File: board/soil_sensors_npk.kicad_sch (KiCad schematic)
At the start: 0 parts

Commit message: added NPK and soil sensors pt. 1
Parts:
- added Conn16: Molex_uF_D_04, MRDT_Connectors:MOLEX_uF_D_04_Horizontal, symbol MRDT_Connectors:Molex_uF_D_04
- added Conn9: Molex_SL_03, symbol MRDT_Connectors:Molex_SL_03
- added R5: 120, symbol Device:R_US
- added U6: MAX3485, Package_SO:SOIC-8_3.9x4.9mm_P1.27mm, symbol Interface_UART:MAX3485
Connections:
- new net: Conn16.2, R5.1, U6.6 (A)
- new net: Conn16.3, R5.2, U6.7 (B)
- new net +3.3V: U6.8 (VCC)
- new net +5V: Conn16.1
- new net DE: U6.3 (DE)
- new net DI: U6.4 (DI)
- new net GND: Conn16.4, U6.5 (GND)
- new net RE: U6.2 (~{RE})
- new net RO: U6.1 (RO)

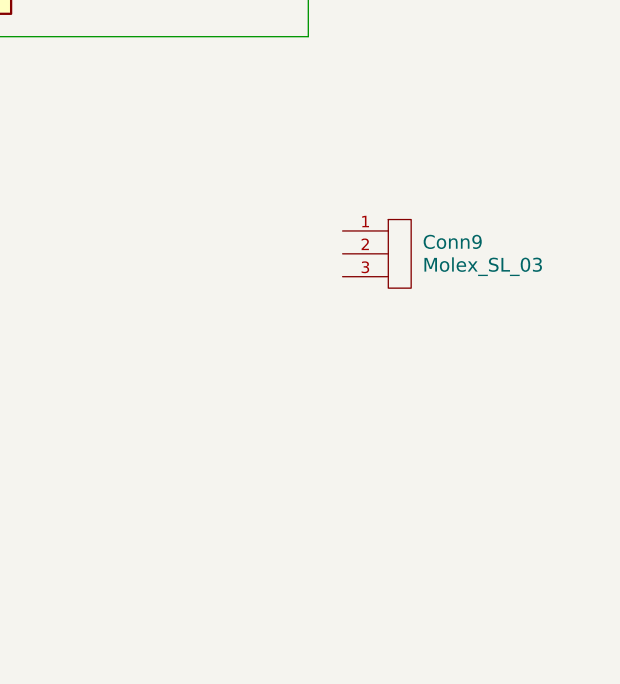
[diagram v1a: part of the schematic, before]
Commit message: Soil sensors pt. 2
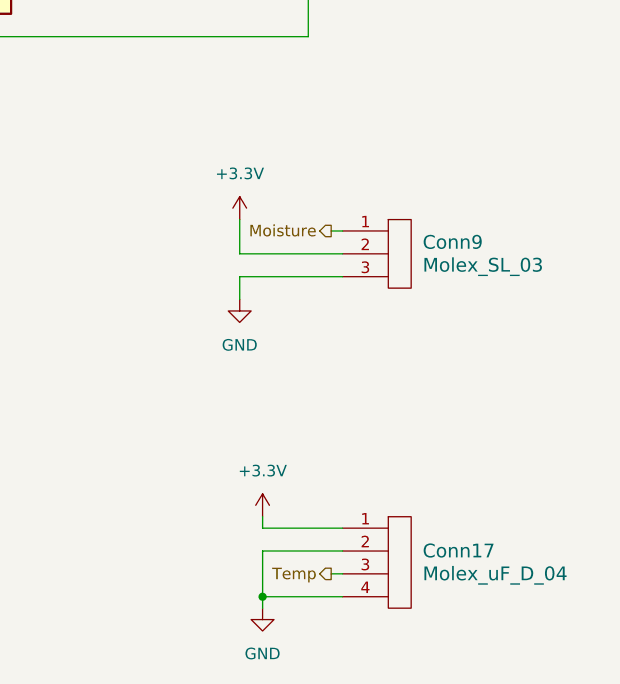
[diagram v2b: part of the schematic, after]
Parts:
- added Conn17: Molex_uF_D_04, MRDT_Connectors:MOLEX_uF_D_04_Horizontal, symbol MRDT_Connectors:Molex_uF_D_04
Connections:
- net +3.3V: now also Conn9.2, Conn17.1
- net GND: now also Conn9.3, Conn17.2, Conn17.4
- net Moisture: now reaches Conn9.1
- new net Temp: Conn17.3

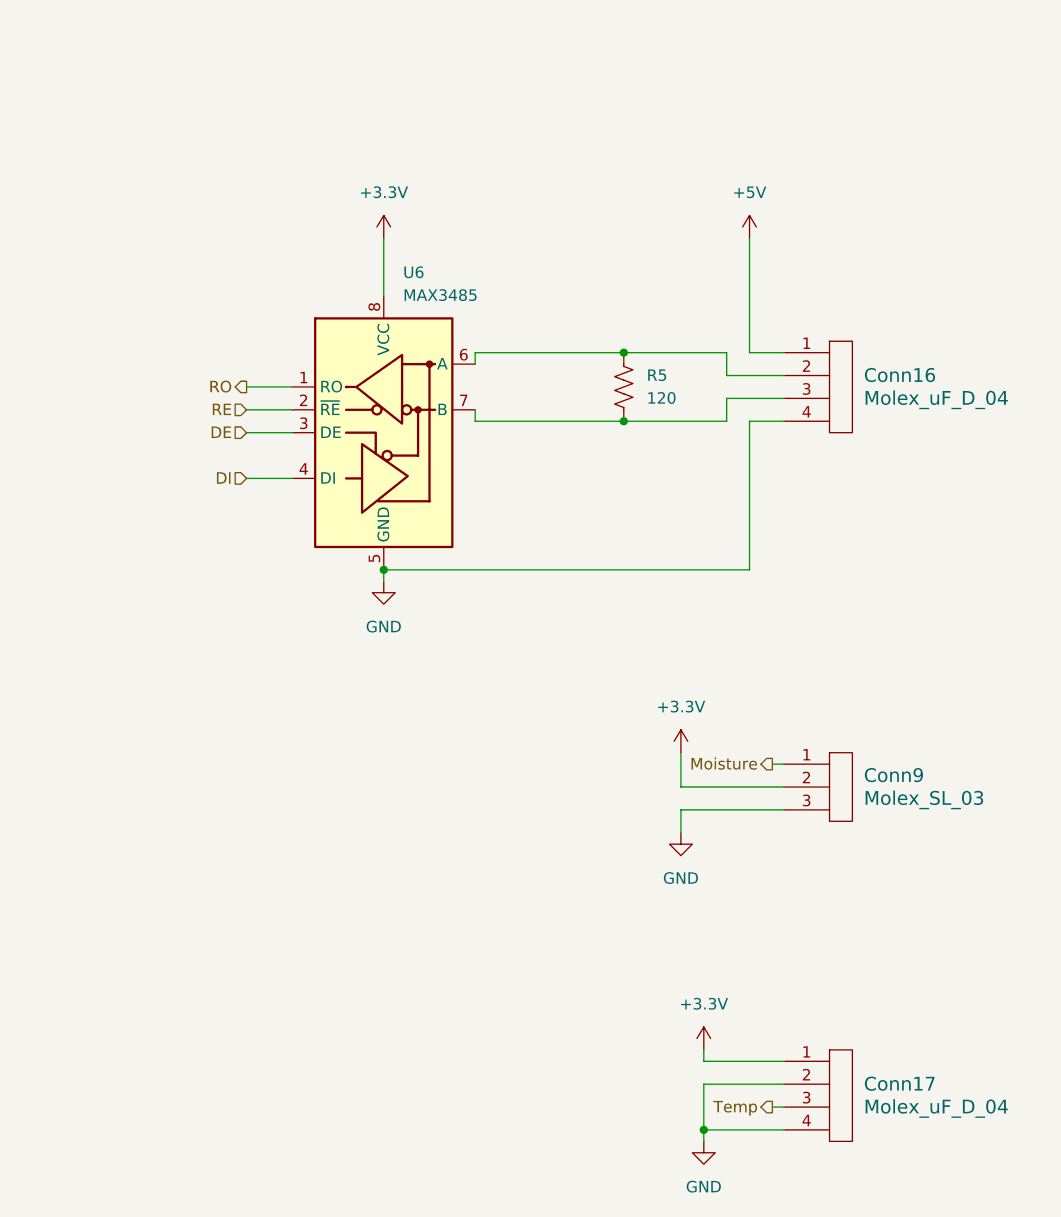
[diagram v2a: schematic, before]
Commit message: Added Labels, Missing Requirements, and Refined Look
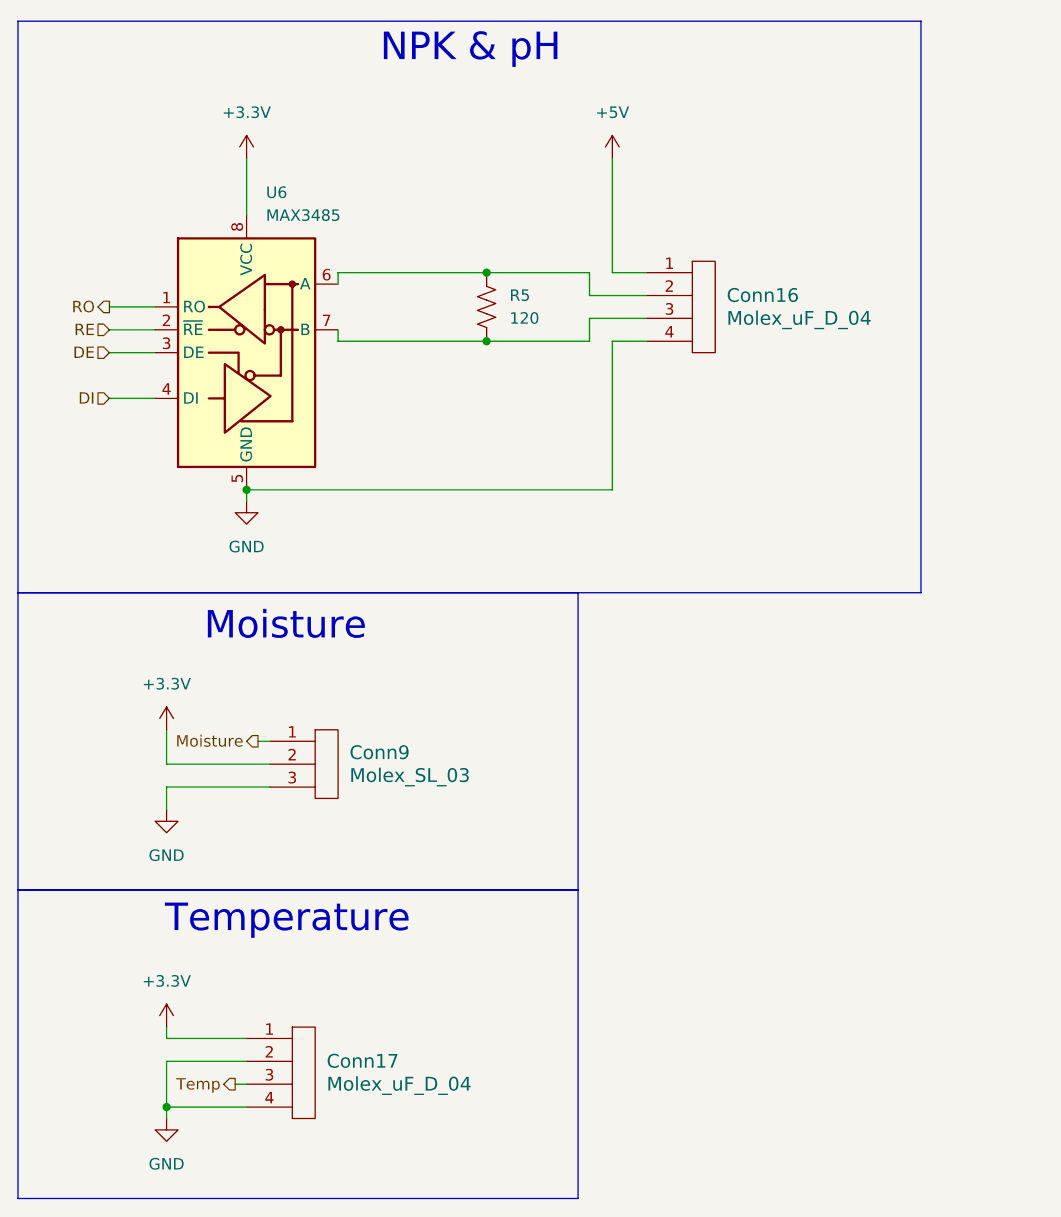
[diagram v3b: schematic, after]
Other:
- note added: "Moisture"
- note added: "NPK & pH"
- note added: "Temperature"
- moved on the sheet: Conn16, Conn17, Conn9, R5, U6

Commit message: assigned footprints
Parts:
- Conn9: footprint (none) -> MRDT_Connectors:MOLEX_SL_03_Vertical
- R5: footprint (none) -> Resistor_SMD:R_0603_1608Metric_Pad0.98x0.95mm_HandSolder
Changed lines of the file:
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@@
 			)
 		)
-		(property "Footprint" ""
+		(property "Footprint" "Resistor_SMD:R_0603_1608Metric_Pad0.98x0.95mm_HandSolder"
 			(at 65.786 44.704 90)
 			(effects
@@
 			)
 		)
-		(property "Footprint" ""
+		(property "Footprint" "MRDT_Connectors:MOLEX_SL_03_Vertical"
 			(at 45.72 99.06 0)
 			(effects

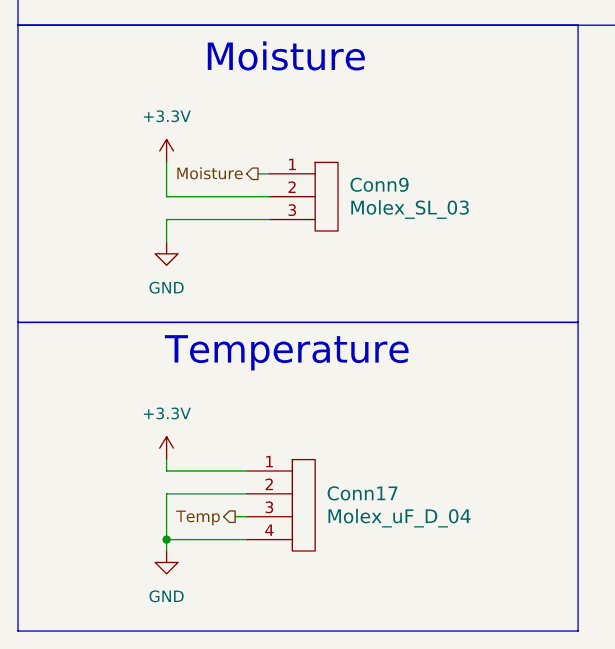
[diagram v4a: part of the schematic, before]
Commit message: Fixed issues after schematic review
added 6 leds for every servo, changed txd and rxd to pins 30/31, added additional oki for 3.3V
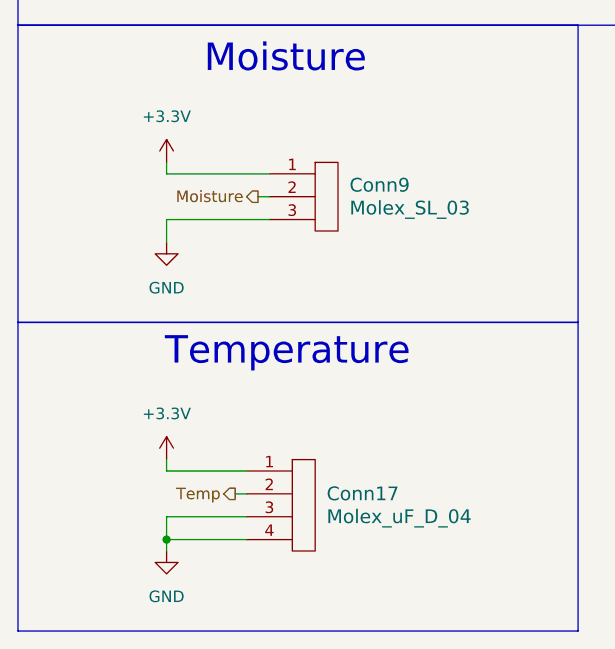
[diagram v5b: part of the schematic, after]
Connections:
- net +3.3V: now also Conn9.1; no longer Conn9.2
- net GND: now also Conn17.3; no longer Conn17.2
- net Moisture: now also Conn9.2; no longer Conn9.1
- net Temp: now also Conn17.2; no longer Conn17.3
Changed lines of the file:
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@@
+	)
+	(junction
+		(at 64.77 40.64)
+		(diameter 0)
+		(color 0 0 0 0)
 	)
 	(junction
@@
 		(color 0 0 0 0)
 	)
-	(junction
-		(at 64.77 40.64)
-		(diameter 0)
-		(color 0 0 0 0)
-	)
 	(wire
 		(pts
@@
 	(wire
 		(pts
+			(xy 39.37 95.25) (xy 40.64 95.25)
+		)
+		(stroke
+			(width 0)
+			(type default)
+		)
+	)
+	(wire
+		(pts
 			(xy 76.2 40.64) (xy 64.77 40.64)
 		)
@@
 	(wire
 		(pts
-			(xy 38.1 128.27) (xy 29.21 128.27)
+			(xy 36.83 128.27) (xy 38.1 128.27)
+		)
+		(stroke
+			(width 0)
+			(type default)
+		)
+	)
+	(wire
+		(pts
+			(xy 29.21 92.71) (xy 40.64 92.71)
 		)
 		(stroke
@@
 	(wire
 		(pts
-			(xy 38.1 133.35) (xy 29.21 133.35)
-		)
-		(stroke
-			(width 0)
-			(type default)
-		)
-	)
-	(wire
-		(pts
 			(xy 22.86 49.53) (xy 27.94 49.53)
 		)
@@
 	(wire
 		(pts
-			(xy 29.21 95.25) (xy 29.21 91.44)
-		)
-		(stroke
-			(width 0)
-			(type default)
-		)
-	)
-	(wire
-		(pts
 			(xy 48.26 46.99) (xy 48.26 48.26)
 		)
@@
 	(wire
 		(pts
-			(xy 40.64 95.25) (xy 29.21 95.25)
-		)
-		(stroke
-			(width 0)
-			(type default)
-		)
-	)
-	(wire
-		(pts
 			(xy 38.1 27.94) (xy 38.1 34.29)
 		)
@@
 	(wire
 		(pts
+			(xy 29.21 130.81) (xy 29.21 133.35)
+		)
+		(stroke
+			(width 0)
+			(type default)
+		)
+	)
+	(wire
+		(pts
+			(xy 29.21 91.44) (xy 29.21 92.71)
+		)
+		(stroke
+			(width 0)
+			(type default)
+		)
+	)
+	(wire
+		(pts
 			(xy 40.64 97.79) (xy 29.21 97.79)
 		)
@@
 	(wire
 		(pts
+			(xy 29.21 133.35) (xy 38.1 133.35)
+		)
+		(stroke
+			(width 0)
+			(type default)
+		)
+	)
+	(wire
+		(pts
 			(xy 76.2 43.18) (xy 76.2 40.64)
 		)
@@
 	(wire
 		(pts
-			(xy 39.37 92.71) (xy 40.64 92.71)
+			(xy 38.1 130.81) (xy 29.21 130.81)
 		)
 		(stroke
@@
 	(wire
 		(pts
-			(xy 29.21 128.27) (xy 29.21 133.35)
-		)
-		(stroke
-			(width 0)
-			(type default)
-		)
-	)
-	(wire
-		(pts
 			(xy 76.2 43.18) (xy 82.55 43.18)
 		)
@@
 		(pts
 			(xy 22.86 46.99) (xy 27.94 46.99)
-		)
-		(stroke
-			(width 0)
-			(type default)
-		)
-	)
-	(wire
-		(pts
-			(xy 36.83 130.81) (xy 38.1 130.81)
 		)
 		(stroke
@@
 	(hierarchical_label "Temp"
 		(shape output)
-		(at 36.83 130.81 180)
+		(at 36.83 128.27 180)
 		(effects
 			(font
@@
 	(hierarchical_label "Moisture"
 		(shape output)
-		(at 39.37 92.71 180)
+		(at 39.37 95.25 180)
 		(effects
 			(font

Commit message: switched soil sensor ports and layout work
soil sensor ports in fact needed to be the way they were originally after looking into the sensors we are using. Also started moving different components on layout to their spots.
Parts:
- removed Conn17: Molex_uF_D_04, MRDT_Connectors:MOLEX_uF_D_04_Horizontal, symbol MRDT_Connectors:Molex_uF_D_04
- added J2: Conn_01x04_MountingPin, symbol Connector_Generic_MountingPin:Conn_01x04_MountingPin
- Conn16: footprint MRDT_Connectors:MOLEX_uF_D_04_Horizontal -> MRDT_Connectors:MOLEX_SL_04_Vertical
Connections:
- net +3.3V: now also Conn9.2, J2.1 (Pin_1); no longer Conn9.1
- net GND: now also J2.2 (Pin_2), J2.4 (Pin_4)
- net Moisture: now also Conn9.1; no longer Conn9.2
- net Temp: now also J2.3 (Pin_3)
- no-connect marks 0 -> 1
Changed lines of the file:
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@@
 		(color 0 0 0 0)
 	)
+	(no_connect
+		(at 43.18 138.43)
+	)
 	(wire
 		(pts
@@
 	(wire
 		(pts
-			(xy 39.37 95.25) (xy 40.64 95.25)
+			(xy 36.83 130.81) (xy 38.1 130.81)
+		)
+		(stroke
+			(width 0)
+			(type default)
+		)
+	)
+	(wire
+		(pts
+			(xy 39.37 92.71) (xy 40.64 92.71)
+		)
+		(stroke
+			(width 0)
+			(type default)
+		)
+	)
+	(wire
+		(pts
+			(xy 40.64 95.25) (xy 29.21 95.25)
 		)
 		(stroke
@@
 	(wire
 		(pts
-			(xy 36.83 128.27) (xy 38.1 128.27)
-		)
-		(stroke
-			(width 0)
-			(type default)
-		)
-	)
-	(wire
-		(pts
-			(xy 29.21 92.71) (xy 40.64 92.71)
-		)
-		(stroke
-			(width 0)
-			(type default)
-		)
-	)
-	(wire
-		(pts
 			(xy 38.1 125.73) (xy 29.21 125.73)
 		)
@@
 	(wire
 		(pts
+			(xy 38.1 128.27) (xy 29.21 128.27)
+		)
+		(stroke
+			(width 0)
+			(type default)
+		)
+	)
+	(wire
+		(pts
 			(xy 76.2 45.72) (xy 82.55 45.72)
 		)
@@
 	(wire
 		(pts
-			(xy 29.21 130.81) (xy 29.21 133.35)
-		)
-		(stroke
-			(width 0)
-			(type default)
-		)
-	)
-	(wire
-		(pts
-			(xy 29.21 91.44) (xy 29.21 92.71)
+			(xy 29.21 128.27) (xy 29.21 133.35)
+		)
+		(stroke
+			(width 0)
+			(type default)
+		)
+	)
+	(wire
+		(pts
+			(xy 29.21 91.44) (xy 29.21 95.25)
 		)
 		(stroke
@@
 	(wire
 		(pts
-			(xy 38.1 130.81) (xy 29.21 130.81)
-		)
-		(stroke
-			(width 0)
-			(type default)
-		)
-	)
-	(wire
-		(pts
 			(xy 78.74 48.26) (xy 82.55 48.26)
 		)
@@
 	(wire
 		(pts
-			(xy 76.2 48.26) (xy 76.2 45.72)
+			(xy 76.2 45.72) (xy 76.2 48.26)
 		)
 		(stroke
@@
 	(hierarchical_label "Temp"
 		(shape output)
-		(at 36.83 128.27 180)
+		(at 36.83 130.81 180)
 		(effects
 			(font
@@
 	(hierarchical_label "Moisture"
 		(shape output)
-		(at 39.37 95.25 180)
+		(at 39.37 92.71 180)
 		(effects
 			(font
@@
 			)
 		)
-		(property "Footprint" "MRDT_Connectors:MOLEX_uF_D_04_Horizontal"
+		(property "Footprint" "MRDT_Connectors:MOLEX_SL_04_Vertical"
 			(at 87.63 49.53 0)
 			(effects
@@
 				(path "/05fd3c2e-b986-4426-9c38-2a77d5c929de/f1c20728-7c40-49e0-910a-0c2b6b14cbc0"
 					(reference "Conn16")
-					(unit 1)
-				)
-			)
-		)
-	)
-	(symbol
-		(lib_id "MRDT_Connectors:Molex_uF_D_04")
-		(at 43.18 134.62 0)
-		(unit 1)
-		(exclude_from_sim no)
-		(in_bom yes)
-		(on_board yes)
-		(dnp no)
-		(fields_autoplaced yes)
-		(property "Reference" "Conn17"
-			(at 46.99 128.2699 0)
-			(effects
-				(font
-					(size 1.524 1.524)
-				)
-				(justify left)
-			)
-		)
-		(property "Value" "Molex_uF_D_04"
-			(at 46.99 130.8099 0)
-			(effects
-				(font
-					(size 1.524 1.524)
-				)
-				(justify left)
-			)
-		)
-		(property "Footprint" "MRDT_Connectors:MOLEX_uF_D_04_Horizontal"
-			(at 43.18 134.62 0)
-			(effects
-				(font
-					(size 1.524 1.524)
-				)
-				(hide yes)
-			)
-		)
-		(property "Datasheet" ""
-			(at 43.18 134.62 0)
-			(effects
-				(font
-					(size 1.524 1.524)
-				)
-				(hide yes)
-			)
-		)
-		(property "Description" ""
-			(at 43.18 134.62 0)
-			(effects
-				(font
-					(size 1.27 1.27)
-				)
-				(hide yes)
-			)
-		)
-		(pin "1"
-		)
-		(pin "2"
-		)
-		(pin "3"
-		)
-		(pin "4"
-		)
-		(instances
-			(project ""
-				(path "/05fd3c2e-b986-4426-9c38-2a77d5c929de/f1c20728-7c40-49e0-910a-0c2b6b14cbc0"
-					(reference "Conn17")
 					(unit 1)
 				)
@@
 					(unit 1)
 				)
+			)
+		)
+	)
+	(symbol
+		(lib_id "Connector_Generic_MountingPin:Conn_01x04_MountingPin")
+		(at 43.18 128.27 0)
+		(unit 1)
+		(exclude_from_sim no)
+		(in_bom yes)
+		(on_board yes)
+		(dnp no)
+		(fields_autoplaced yes)
+		(property "Reference" "J2"
+			(at 45.72 128.6255 0)
+			(effects
+				(font
+					(size 1.27 1.27)
+				)
+				(justify left)
+			)
+		)
+		(property "Value" "Conn_01x04_MountingPin"
+			(at 45.72 131.1655 0)
+			(effects
+				(font
+					(size 1.27 1.27)
+				)
+				(justify left)
+			)
+		)
+		(property "Footprint" ""
+			(at 43.18 128.27 0)
+			(effects
+				(font
+					(size 1.27 1.27)
+				)
+				(hide yes)
+			)
+		)
+		(property "Datasheet" "~"
+			(at 43.18 128.27 0)
+			(effects
+				(font
+					(size 1.27 1.27)
+				)
+				(hide yes)
+			)
+		)
+		(property "Description" "Generic connectable mounting pin connector, single row, 01x04, script generated (kicad-library-utils/schlib/autogen/connector/)"
+			(at 43.18 128.27 0)
+			(effects
+				(font
+					(size 1.27 1.27)
+				)
+				(hide yes)
+			)
+		)
+		(pin "1"
+		)
+		(pin "2"
+		)
+		(pin "4"
+		)
+		(pin "3"
+		)
+		(pin "MP"
+		)
+		(instances
+			(project ""
+				(path "/05fd3c2e-b986-4426-9c38-2a77d5c929de/f1c20728-7c40-49e0-910a-0c2b6b14cbc0"
+					(reference "J2")
+					(unit 1)
+				)

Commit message: Layout Progress
Made a basic setup for locations, placed preliminary wires and text, rearranged teensy pins for simplicity
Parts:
- J2: footprint (none) -> Connector_PinHeader_2.54mm:PinHeader_1x04_P2.54mm_Vertical
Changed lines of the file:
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@@
 			)
 		)
-		(property "Footprint" ""
+		(property "Footprint" "Connector_PinHeader_2.54mm:PinHeader_1x04_P2.54mm_Vertical"
 			(at 43.18 128.27 0)
 			(effects

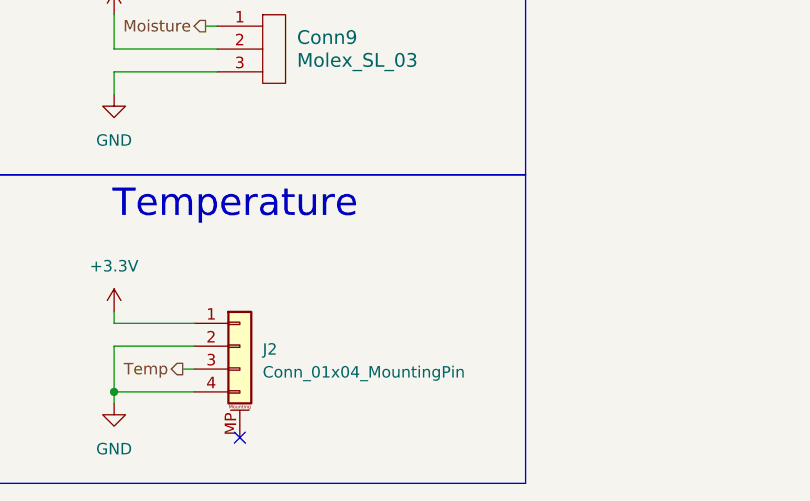
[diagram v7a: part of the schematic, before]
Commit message: Add reverse voltage protection circuit
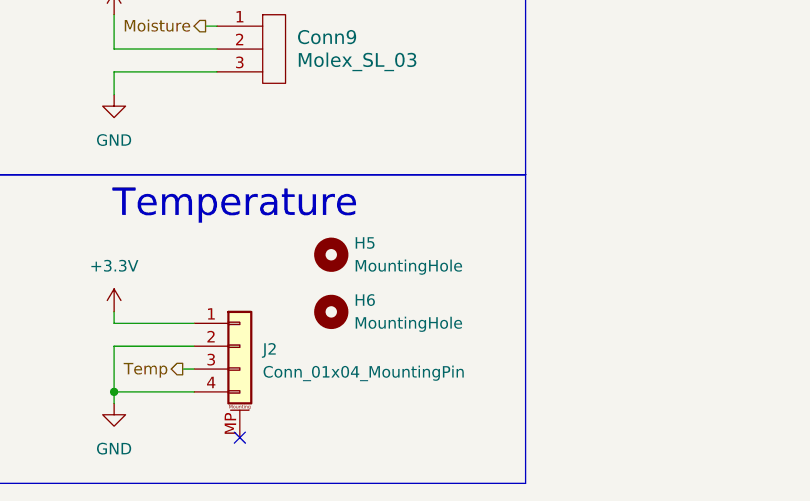
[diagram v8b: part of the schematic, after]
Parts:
- added H5, H6: MountingHole, MountingHole:MountingHole_2.7mm, symbol Mechanical:MountingHole
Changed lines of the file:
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@@
+	)
+	(symbol
+		(lib_id "Mechanical:MountingHole")
+		(at 53.34 124.46 0)
+		(unit 1)
+		(exclude_from_sim no)
+		(in_bom no)
+		(on_board yes)
+		(dnp no)
+		(fields_autoplaced yes)
+		(property "Reference" "H6"
+			(at 55.88 123.1899 0)
+			(effects
+				(font
+					(size 1.27 1.27)
+				)
+				(justify left)
+			)
+		)
+		(property "Value" "MountingHole"
+			(at 55.88 125.7299 0)
+			(effects
+				(font
+					(size 1.27 1.27)
+				)
+				(justify left)
+			)
+		)
+		(property "Footprint" "MountingHole:MountingHole_2.7mm"
+			(at 53.34 124.46 0)
+			(effects
+				(font
+					(size 1.27 1.27)
+				)
+				(hide yes)
+			)
+		)
+		(property "Datasheet" "~"
+			(at 53.34 124.46 0)
+			(effects
+				(font
+					(size 1.27 1.27)
+				)
+				(hide yes)
+			)
+		)
+		(property "Description" "Mounting Hole without connection"
+			(at 53.34 124.46 0)
+			(effects
+				(font
+					(size 1.27 1.27)
+				)
+				(hide yes)
+			)
+		)
+		(instances
+			(project "AugerBoard"
+				(path "/05fd3c2e-b986-4426-9c38-2a77d5c929de/f1c20728-7c40-49e0-910a-0c2b6b14cbc0"
+					(reference "H6")
+					(unit 1)
+				)
+			)
+		)
 	)
 	(symbol
@@
 					(unit 1)
 				)
+			)
+		)
+	)
+	(symbol
+		(lib_id "Mechanical:MountingHole")
+		(at 53.34 118.11 0)
+		(unit 1)
+		(exclude_from_sim no)
+		(in_bom no)
+		(on_board yes)
+		(dnp no)
+		(fields_autoplaced yes)
+		(property "Reference" "H5"
+			(at 55.88 116.8399 0)
+			(effects
+				(font
+					(size 1.27 1.27)
+				)
+				(justify left)
+			)
+		)
+		(property "Value" "MountingHole"
+			(at 55.88 119.3799 0)
+			(effects
+				(font
+					(size 1.27 1.27)
+				)
+				(justify left)
+			)
+		)
+		(property "Footprint" "MountingHole:MountingHole_2.7mm"
+			(at 53.34 118.11 0)
+			(effects
+				(font
+					(size 1.27 1.27)
+				)
+				(hide yes)
+			)
+		)
+		(property "Datasheet" "~"
+			(at 53.34 118.11 0)
+			(effects
+				(font
+					(size 1.27 1.27)
+				)
+				(hide yes)
+			)
+		)
+		(property "Description" "Mounting Hole without connection"
+			(at 53.34 118.11 0)
+			(effects
+				(font
+					(size 1.27 1.27)
+				)
+				(hide yes)
+			)
+		)
+		(instances
+			(project "AugerBoard"
+				(path "/05fd3c2e-b986-4426-9c38-2a77d5c929de/f1c20728-7c40-49e0-910a-0c2b6b14cbc0"
+					(reference "H5")
+					(unit 1)
+				)
